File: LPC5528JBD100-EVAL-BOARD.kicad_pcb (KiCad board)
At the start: 2 copper layers, 100 x 100 mm, 78 parts, among them J1 Barrel_Jack_MountingPin, J2 USB_B_Micro, J3 ADC_EXT_SUPPLY, J4 MCU_V_SEL, J5 JLink-1, J6 JLink-2, J7 Conn_01x40, J8 Conn_02x20, J9 VBus-Select, SW1 SW_SPST, U1 LM2596S-5, U2 LPC55S28JBD100, U3 LM1117-3.3, U4 LM1117-1.8, U5 TPS2552DBVR, Y1 16MHz

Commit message: JTAG swo pin pull down yapıldı
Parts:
- added R18: 100k, Resistor_SMD:R_0603_1608Metric, F.Cu at (164.8, 13.7)
- added R19: 100, Resistor_SMD:R_0603_1608Metric, F.Cu at (159.1, 11.2)
- added SW2: SW_SPST, Button_Switch_SMD:SW_SPST_PTS645, F.Cu at (141.2, 13.8)
- J7: value Conn_01x40 -> Conn_02x20; footprint Connector_PinSocket_2.54mm:PinSocket_1x40_P2.54mm_Vertical -> Connector_PinSocket_2.54mm:PinSocket_2x20_P2.54mm_Vertical
- moved J3 144.6 mm to (180.6, 37.1)
- moved TP1 143.8 mm to (207.0, 16.2)
- moved C6 131.2 mm to (167.2, 11.2), turned to 0 degrees
- moved TP5 117.5 mm to (193.6, 29.0)
- moved C7 116.1 mm to (147.1, 19.0)
- moved U4 113.4 mm to (178.5, 24.7)
- moved U3 107.7 mm to (187.5, 14.1)
- moved J9 86.9 mm to (121.8, -1.38)
- moved J5 85.5 mm to (137.7, 19.4), turned to 0 degrees
- moved SW1 84.0 mm to (129.2, 36.3)
- moved C30 82.6 mm to (180.2, 48.2)
- moved R9 82.6 mm to (184.2, 48.2)
- moved R7 81.8 mm to (188.2, 46.1)
- moved C9 80.6 mm to (175.6, 48.5)
- moved R8 80.2 mm to (184.9, 41.1)
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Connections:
- J9 pad 2: unconnected-(J9-Pad2) -> VBUS
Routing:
- net /MCU_1/MCU_XTAL32M_P: track 12.5 -> 0.00 mm
- net /MCU_1/MCU_XTAL32M_N: track 10.4 -> 0.00 mm
- net (no net): track 1.24 -> 0.00 mm

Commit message: Butonlar eklendi
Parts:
- removed C12: 10nF, Capacitor_SMD:C_0603_1608Metric
- removed the C7 at (147.1, 19.0)
- removed the C8 at (192.9, 41.1)
- removed the J3 at (180.6, 37.1)
- removed the R5 at (198.1, 23.7)
- removed the TP1 at (207.0, 16.2)
- removed the TP4 at (202.5, 19.2)
- removed the U3 at (187.5, 14.1)
- removed the U5 at (178.2, 16.2)
- added C24: 10nF, Capacitor_SMD:C_0603_1608Metric, F.Cu at (196.0, 13.6)
- added C3: 0.1uF, Capacitor_SMD:C_0603_1608Metric, F.Cu at (140.1, 62.8)
- added C5: 10uF, Capacitor_Tantalum_SMD:CP_EIA-6032-28_Kemet-C, F.Cu at (156.9, 45.0)
- added J1: VBus-Select, Connector_PinHeader_2.54mm:PinHeader_1x03_P2.54mm_Vertical, F.Cu at (150.3, 45.0)
- added J7: USB_B_Micro, Connector_USB:USB_Micro-B_Molex_47346-0001, F.Cu at (125.2, 75.9)
- added J8: JLink-1, Connector_PinHeader_1.27mm:PinHeader_2x05_P1.27mm_Vertical, F.Cu at (169.1, 14.0)
- added R20: 100k, Resistor_SMD:R_0603_1608Metric, F.Cu at (151.2, 38.1)
- added R21: 100k, Resistor_SMD:R_0603_1608Metric, F.Cu at (131.2, 36.0)
- added R22: 100, Resistor_SMD:R_0603_1608Metric, F.Cu at (147.2, 35.6)
- added R3: 0 Ohm, Resistor_SMD:R_0603_1608Metric, F.Cu at (154.6, 48.6)
- added SW3: USER, Button_Switch_SMD:SW_SPST_PTS645, F.Cu at (146.7, 30.4)
- added SW4: SW_SPST, Button_Switch_SMD:SW_SPST_PTS645, F.Cu at (146.7, 22.5)
- added TP2: TP_5V_EXT, TestPoint:TestPoint_Pad_D1.0mm, F.Cu at (157.7, 53.9)
- added TP3: TP_3V3, TestPoint:TestPoint_Pad_D1.0mm, F.Cu at (147.6, 63.4)
- added U1: TPS2552DBVR, erkan-hw-lib:TPS2552DBVR, F.Cu at (133.8, 48.9)
- added U2: LM1117-3.3, Package_TO_SOT_SMD:SOT-223-3_TabPin2, F.Cu at (143.0, 46.8)
- C10: value 10nF -> 4.7uF
- C11: value 0.1uF -> 22uF
- C14: value 0.1uF -> 100nF
- C16: value 0.1uF -> 47pF
- C17, C19: value 10uF -> 0.1uF; footprint Capacitor_Tantalum_SMD:CP_EIA-6032-28_Kemet-C -> Capacitor_SMD:C_0603_1608Metric
- C18: value 10uF -> 10nF; footprint Capacitor_Tantalum_SMD:CP_EIA-6032-28_Kemet-C -> Capacitor_SMD:C_0603_1608Metric
- C20: value 120uF -> 0.1uF; footprint Capacitor_Tantalum_SMD:CP_EIA-6032-28_Kemet-C -> Capacitor_SMD:C_0603_1608Metric
- C21: value 47pF -> 10nF
- C23: value 10nF -> 22uF
- C25, C28: value 22uF -> 47pF
- C27: value 47pF -> 2.2uF
- C29: value 47pF -> 0.1uF
- C30: value 100nF -> 10uF
- C31: value 2.2uF -> 10uF
- C32, C33: value 10uF -> 18pF
- C4, C9: value 0.1uF -> 100uF; footprint Capacitor_SMD:C_0603_1608Metric -> Capacitor_Tantalum_SMD:CP_EIA-6032-28_Kemet-C
- C6: value 18pF -> 120uF; footprint Capacitor_SMD:C_0603_1608Metric -> Capacitor_Tantalum_SMD:CP_EIA-6032-28_Kemet-C
- J3: renamed from J1; value Barrel_Jack_MountingPin -> DC_IN
- J4: value MCU_V_SEL -> ADC_EXT_SUPPLY
- J5: value JLink-1 -> MCU_V_SEL; footprint Connector_PinHeader_1.27mm:PinHeader_2x05_P1.27mm_Vertical -> Connector_PinHeader_2.54mm:PinHeader_1x03_P2.54mm_Vertical
- J6: value JLink-2 -> USB_B_Micro; footprint Connector_IDC:IDC-Header_2x05_P2.54mm_Vertical -> Connector_USB:USB_Micro-B_Molex_47346-0001
- J9: value VBus-Select -> JLink-2; footprint Connector_PinHeader_2.54mm:PinHeader_1x03_P2.54mm_Vertical -> Connector_IDC:IDC-Header_2x05_P2.54mm_Vertical
- R1: value 0 Ohm -> 47k
- R11: value 0 -> 2.2k
- R12: value 0 -> 330k
- R14: value 100k -> 100
- R15, R16: value 100k -> 0
- R17, R19: value 100 -> 100k
- R2: value 1.2k Ohm -> 100k
- R4: value 68 Ohm -> 1.2k Ohm
- R6: value 100k -> 68 Ohm
- SW1: value SW_SPST -> ISP
- SW2: value SW_SPST -> WAKE
- TP5: value TP_5V_EXT -> TP_1V8
- moved D2 75.6 mm to (131.4, 63.0)
- moved C2 71.2 mm to (151.9, 59.5)
- moved J6 60.2 mm to (135.7, 75.9)
- moved D5 60.2 mm to (135.9, 63.0)
- moved Y1 59.6 mm to (148.5, 15.5)
- moved SW1 55.9 mm to (174.0, 2.90)
- moved U4 55.2 mm to (134.1, 57.4)
- moved C6 52.5 mm to (143.4, 58.0)
- moved D3 48.6 mm to (163.5, 44.1)
- moved R1 47.5 mm to (144.1, 61.6)
- moved J5 45.5 mm to (183.0, 14.7)
- moved R6 43.6 mm to (158.2, 51.1)
- moved R2 40.1 mm to (162.6, 48.6)
- moved R4 37.0 mm to (158.6, 48.6)
- moved C11 36.9 mm to (200.0, 13.6)
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- renumbered C3 to C7, C5 to C8, J7 to J10, J8 to J11, R3 to R5, TP6 to TP1, TP2 to TP4, TP3 to TP6, U1 to U3, U2 to U5
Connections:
- C17 pad 1: +3V3 -> V_TARGET
- C18 pad 1: +5V -> V_TARGET
- C19 pad 1: +1V8 -> V_TARGET
- C20 pad 1: VBUS -> V_TARGET
- C23 pad 1: /MCU/VREFP_TARGET -> Net-(C23-Pad1)
- C25 pad 1: V_TARGET -> Net-(C23-Pad1)
- C25 pad 2: GND -> Net-(C23-Pad1)
- C26 pad 1: V_TARGET -> Net-(C23-Pad1)
- C26 pad 2: GND -> Net-(C23-Pad1)
- C27 pad 1: V_TARGET -> Net-(C23-Pad1)
- C27 pad 2: GND -> Net-(C23-Pad1)
- C28 pad 1: Net-(C28-Pad1) -> V_TARGET
- C29 pad 1: Net-(C28-Pad1) -> V_TARGET
- C29 pad 2: Net-(C28-Pad1) -> GND
- C30 pad 1: Net-(C28-Pad1) -> V_TARGET
- C30 pad 2: Net-(C28-Pad1) -> GND
- C31 pad 1: Net-(C28-Pad1) -> /MCU_1/LPC_RESET
- C31 pad 2: Net-(C28-Pad1) -> GND
- C32 pad 1: V_TARGET -> /MCU_1/MCU_XTAL32M_P
- C33 pad 1: /MCU_1/LPC_RESET -> /MCU_1/MCU_XTAL32M_N
- C4 pad 1: +5V -> +3V3
- C6 pad 1: /MCU_1/MCU_XTAL32M_P -> VBUS
- C9 pad 1: V_TARGET -> +1V8
- J4 pad 1: +3V3 -> /MCU/ADC_VREFN
- J4 pad 2: V_TARGET -> GND
- J4 pad 3: +1V8 -> /MCU/ADC_VREFP
- J5 pad 1: V_TARGET -> +3V3
- J5 pad 2: /MCU_1/TMS/SWDIO -> V_TARGET
- J5 pad 3: GND -> +1V8
- J6 pad 1: V_TARGET -> unconnected-(J6-Pad1)
- J6 pad 2: /MCU_1/TMS/SWDIO -> unconnected-(J6-Pad2)
- J6 pad 3: GND -> unconnected-(J6-Pad3)
- J6 pad 4: /MCU_1/TCK/SWCLK -> unconnected-(J6-Pad4)
- J6 pad 5: GND -> unconnected-(J6-Pad5)
- J6 pad 6: /MCU_1/TDO/SWO -> unconnected-(J6-Pad6)
- J9 pad 1: unconnected-(J9-Pad1) -> V_TARGET
- J9 pad 2: VBUS -> /MCU_1/TMS/SWDIO
- J9 pad 3: unconnected-(J9-Pad3) -> GND
- L2 pad 2: Net-(C28-Pad1) -> Net-(C23-Pad1)
- R1 pad 1: Net-(D2-Pad2) -> /Power/USB_ILIM
- R1 pad 2: +1V8 -> GND
- R11 pad 1: /MCU_1/P0_5-ISP1 -> V_TARGET
- R11 pad 2: GND -> /MCU_1/P0_5-ISP1
- R12 pad 1: /MCU_1/GND_DETECT -> V_TARGET
- R12 pad 2: GND -> /MCU_1/WAKE/GPIO
- R13 pad 1: /MCU_1/TMS/SWDIO -> V_TARGET
- R13 pad 2: V_TARGET -> /MCU_1/PIO1_9
- R14 pad 1: GND -> /MCU_1/PIO1_9
- R14 pad 2: /MCU_1/TCK/SWCLK -> Net-(R14-Pad2)
- R15 pad 1: /MCU_1/TCK/SWCLK -> /MCU_1/P0_5-ISP1
- R15 pad 2: V_TARGET -> GND
- R16 pad 1: V_TARGET -> /MCU_1/GND_DETECT
- R16 pad 2: /MCU_1/LPC_RESET -> GND
- R17 pad 1: /MCU_1/LPC_RESET -> /MCU_1/TMS/SWDIO
- R17 pad 2: Net-(R17-Pad2) -> V_TARGET
- R18 pad 1: V_TARGET -> /MCU_1/TDI/N.C.
- R18 pad 2: /MCU_1/P0_5-ISP1 -> GND
- R19 pad 1: Net-(R19-Pad1) -> GND
- R19 pad 2: /MCU_1/P0_5-ISP1 -> /MCU_1/TCK/SWCLK
- R2 pad 1: Net-(D3-Pad2) -> +5V
- R2 pad 2: V_IN -> /Power/USB_FAULT
- R4 pad 1: Net-(D5-Pad2) -> Net-(D3-Pad2)
- R4 pad 2: +3V3 -> V_IN
- R6 pad 1: +5V -> Net-(D5-Pad2)
- R6 pad 2: /Power/USB_FAULT -> +3V3
- SW1 pad 1: Net-(R17-Pad2) -> GND
- SW1 pad 2: GND -> /MCU_1/P0_5-ISP1
- SW2 pad 1: Net-(R19-Pad1) -> GND
- SW2 pad 2: GND -> /MCU_1/WAKE/GPIO
- TP5 pad 1: 5V_EXT -> +1V8
- U5 pad 101: (no net) -> GND
- U5 pad 39: Net-(C28-Pad1) -> Net-(C23-Pad1)
- U5 pad 45: Net-(C28-Pad1) -> Net-(C23-Pad1)
- U5 pad 64: unconnected-(U2-Pad64) -> /MCU_1/WAKE/GPIO
- U5 pad 88: /MCU_1/TDI -> /MCU_1/TDI/N.C.

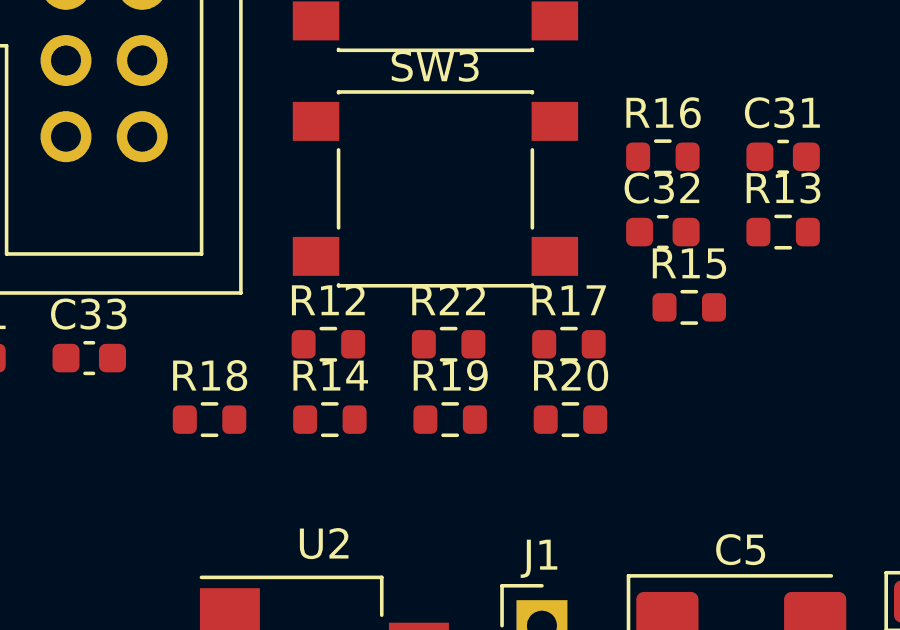
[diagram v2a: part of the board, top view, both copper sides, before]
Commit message: Pin labelları eklendi
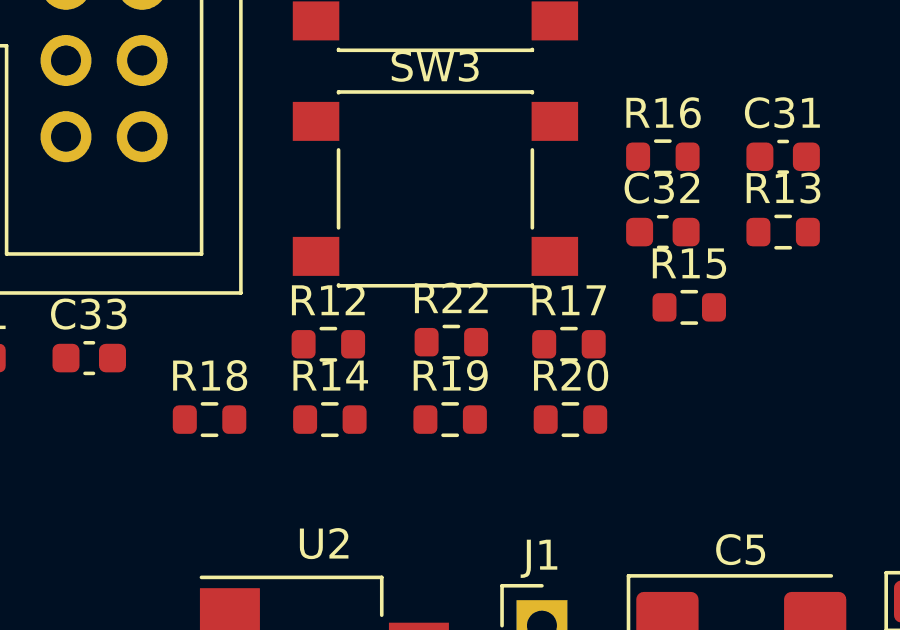
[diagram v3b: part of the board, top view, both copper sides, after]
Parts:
- SW4: value SW_SPST -> MCU_RESET
- moved R22 0.11 mm to (147.3, 35.5)
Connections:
- J1 pad 1: unconnected-(J1-Pad1) -> USB0_VBUS
- J1 pad 3: unconnected-(J1-Pad3) -> USB0_VBUS
- U5 pad 1: unconnected-(U5-Pad1) -> /MCU_1/P1_4
- U5 pad 10: unconnected-(U5-Pad10) -> /MCU_1/P1_9
- U5 pad 11: unconnected-(U5-Pad11) -> /MCU_1/P1_0
- U5 pad 12: unconnected-(U5-Pad12) -> /MCU_1/P0_12
- U5 pad 13: unconnected-(U5-Pad13) -> /MCU_1/P0_11
- U5 pad 14: unconnected-(U5-Pad14) -> /MCU_1/P0_16
- U5 pad 2: unconnected-(U5-Pad2) -> /MCU_1/P1_13
- U5 pad 20: unconnected-(U5-Pad20) -> /MCU_1/P0_23
- U5 pad 21: unconnected-(U5-Pad21) -> /MCU_1/P0_10
- U5 pad 22: unconnected-(U5-Pad22) -> /MCU_1/P0_16
- U5 pad 23: unconnected-(U5-Pad23) -> /MCU_1/P0_31
- U5 pad 24: unconnected-(U5-Pad24) -> /MCU_1/P1_8
- U5 pad 26: unconnected-(U5-Pad26) -> /MCU_1/P0_8
- U5 pad 27: unconnected-(U5-Pad27) -> /MCU_1/P0_27
- U5 pad 3: unconnected-(U5-Pad3) -> /MCU_1/P1_24
- U5 pad 30: unconnected-(U5-Pad30) -> /MCU_1/P1_21
- U5 pad 31: unconnected-(U5-Pad31) -> /MCU_1/P1_15
- U5 pad 4: unconnected-(U5-Pad4) -> /MCU_1/P1_20
- U5 pad 40: unconnected-(U5-Pad40) -> /MCU_1/P1_10
- U5 pad 41: unconnected-(U5-Pad41) -> /MCU_1/P1_22
- U5 pad 42: unconnected-(U5-Pad42) -> /MCU_1/P1_23
- U5 pad 43: unconnected-(U5-Pad43) -> /MCU_1/P1_17
- U5 pad 5: unconnected-(U5-Pad5) -> /MCU_1/P1_16
- U5 pad 54: unconnected-(U5-Pad54) -> /MCU_1/P0_0
- U5 pad 55: unconnected-(U5-Pad55) -> /MCU_1/P0_9
- U5 pad 56: unconnected-(U5-Pad56) -> /MCU_1/P0_18
- U5 pad 57: unconnected-(U5-Pad57) -> /MCU_1/P1_14
- U5 pad 58: unconnected-(U5-Pad58) -> /MCU_1/P1_19
- U5 pad 59: unconnected-(U5-Pad59) -> /MCU_1/P1_1
- U5 pad 6: unconnected-(U5-Pad6) -> /MCU_1/P0_7
- U5 pad 60: unconnected-(U5-Pad60) -> /MCU_1/P0_26
- U5 pad 61: unconnected-(U5-Pad61) -> /MCU_1/P1_2
- U5 pad 62: unconnected-(U5-Pad62) -> /MCU_1/P1_3
- U5 pad 65: unconnected-(U5-Pad65) -> /MCU_1/P1_30
- U5 pad 66: unconnected-(U5-Pad66) -> /MCU_1/P0_28
- U5 pad 67: unconnected-(U5-Pad67) -> /MCU_1/P1_12
- U5 pad 68: unconnected-(U5-Pad68) -> /MCU_1/P1_26
- U5 pad 7: unconnected-(U5-Pad7) -> /MCU_1/P0_1
- U5 pad 70: unconnected-(U5-Pad70) -> /MCU_1/P0_24
- U5 pad 71: unconnected-(U5-Pad71) -> /MCU_1/P0_13
- U5 pad 72: unconnected-(U5-Pad72) -> /MCU_1/P0_14
- U5 pad 73: unconnected-(U5-Pad73) -> /MCU_1/P1_28
- U5 pad 74: unconnected-(U5-Pad74) -> /MCU_1/P0_20
- U5 pad 76: unconnected-(U5-Pad76) -> /MCU_1/P0_21
- U5 pad 77: unconnected-(U5-Pad77) -> /MCU_1/P1_25
- U5 pad 78: unconnected-(U5-Pad78) -> /MCU_1/P0_22
- U5 pad 79: unconnected-(U5-Pad79) -> /MCU_1/P0_25
- U5 pad 8: unconnected-(U5-Pad8) -> /MCU_1/P0_7
- U5 pad 80: unconnected-(U5-Pad80) -> /MCU_1/P1_29
- U5 pad 82: unconnected-(U5-Pad82) -> /MCU_1/P1_15
- U5 pad 85: unconnected-(U5-Pad85) -> /MCU_1/P1_27
- U5 pad 87: unconnected-(U5-Pad87) -> /MCU_1/P1_16
- U5 pad 9: unconnected-(U5-Pad9) -> /MCU_1/P1_7
- U5 pad 90: unconnected-(U5-Pad90) -> /MCU_1/P0_19
- U5 pad 91: unconnected-(U5-Pad91) -> /MCU_1/P1_31
- U5 pad 92: unconnected-(U5-Pad92) -> /MCU_1/P0_29
- U5 pad 93: unconnected-(U5-Pad93) -> /MCU_1/P1_11
- U5 pad 94: unconnected-(U5-Pad94) -> /MCU_1/P0_30
